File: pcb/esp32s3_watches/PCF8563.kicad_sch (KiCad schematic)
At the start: 1 part, among them U6 PCF8563TS

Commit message: BOM file updates. Scheme complete.
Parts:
- added BT400: BC2032-E2, esp32s3_watches:MPD_BC2032-E2, symbol esp32s3_watches:BC2032-E2
- added C400: 10uF, Capacitor_SMD:C_0805_2012Metric, symbol Device:C
- added C401: 100nF, Capacitor_SMD:C_0603_1608Metric, symbol Device:C
- added C402: 15pF, Capacitor_SMD:C_0603_1608Metric, symbol Device:C
- added D401, D402: 1N4148, Diode_SMD:D_SOD-123, symbol Device:D
- added R400, R401: 5k1R, Resistor_SMD:R_0805_2012Metric, symbol Device:R
- added Y400: 32768Hz, Crystal:Crystal_SMD_3225-4Pin_3.2x2.5mm, symbol Device:Crystal_GND24
- U400: renamed from U6; Manufacturer (none) -> NXP Semicon; Manufacturer Product Number (none) -> PCF8563TS/5,118
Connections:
- net +3.3V: now also C400.1, C401.1, D402.2 (A), R400.1, R401.1
- net GND: now also U400.2 (OSCO), U400.4 (VSS), BT400.N, C400.2, C401.2, C402.2, Y400.2, Y400.3, Y400.4
- net I2C_SCL: now also U400.6 (SCL), R401.2
- net I2C_SDA: now also U400.5 (SDA), R400.2
- net at U400.1 (OSCI): now also C402.1, Y400.1
- net PCF8563_INT: now reaches U400.3 (~{INT})
- net at U400.8 (VDD): now also D401.1 (K), D402.1 (K)
- new net: BT400.P, D401.2 (A)
- no-connect marks 0 -> 1
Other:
- moved on the sheet: U400

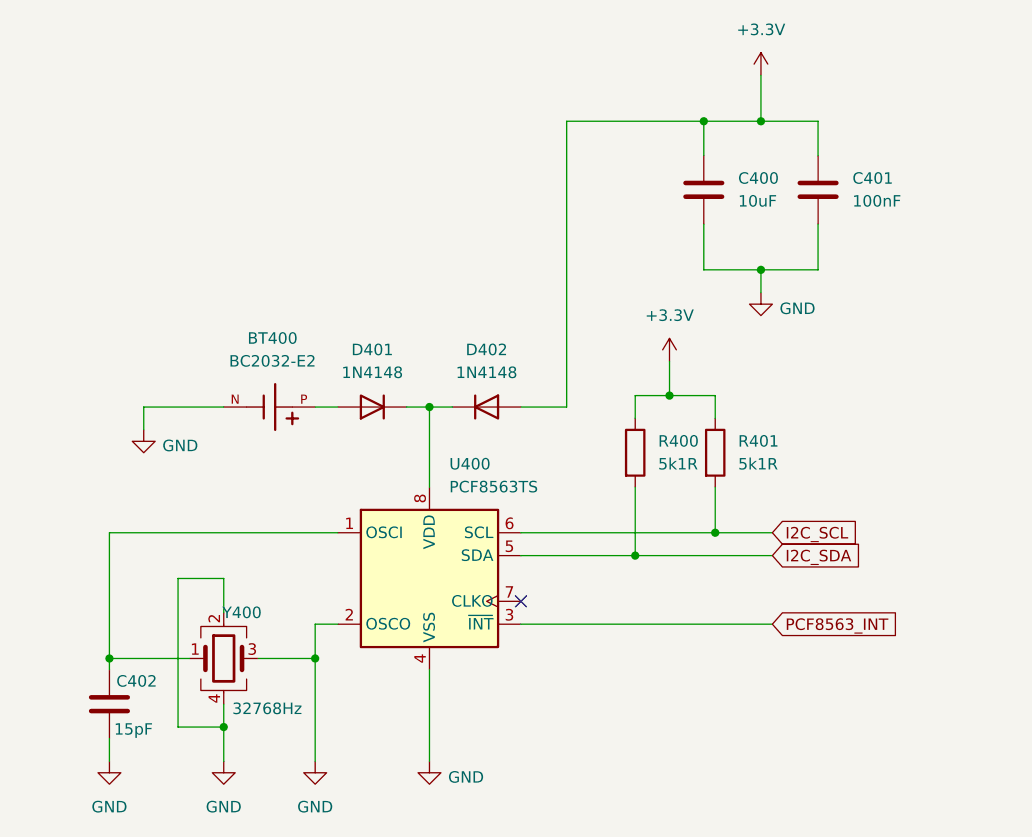
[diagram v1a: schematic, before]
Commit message: PCB initial layout
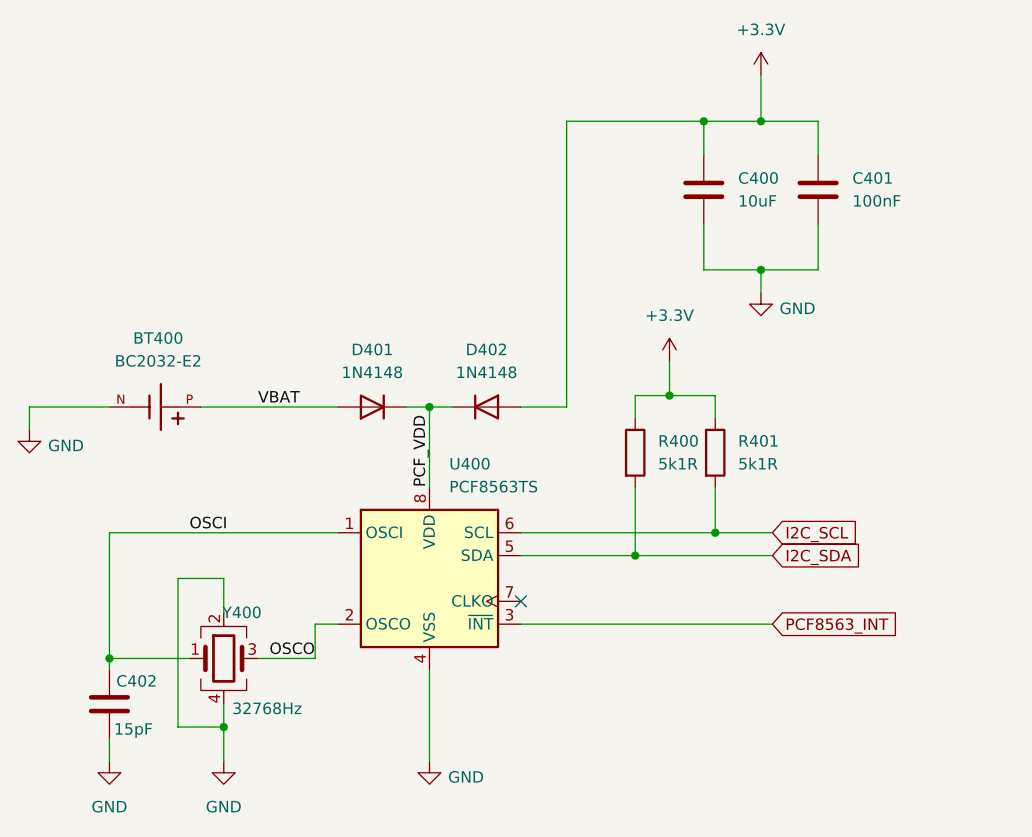
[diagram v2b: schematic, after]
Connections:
- net GND: no longer U400.2 (OSCO), Y400.3
- net VBAT: now reaches BT400.P, D401.2 (A)
- net PCF_VDD: now reaches D401.1 (K), D402.1 (K), U400.8 (VDD)
- net OSCI: now reaches C402.1, U400.1 (OSCI), Y400.1
- new net OSCO: U400.2 (OSCO), Y400.3
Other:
- moved on the sheet: BT400
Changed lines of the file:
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@@
-	)
-	(junction
-		(at 76.2 88.9)
-		(diameter 0)
-		(color 0 0 0 0)
 	)
 	(junction
@@
 	(wire
 		(pts
-			(xy 88.9 69.85) (xy 88.9 60.96)
+			(xy 88.9 60.96) (xy 88.9 69.85)
 		)
 		(stroke
@@
 	(wire
 		(pts
-			(xy 57.15 60.96) (xy 57.15 63.5)
+			(xy 44.45 60.96) (xy 44.45 63.5)
 		)
 		(stroke
@@
 	(wire
 		(pts
-			(xy 76.2 88.9) (xy 76.2 100.33)
-		)
-		(stroke
-			(width 0)
-			(type default)
-		)
-	)
-	(wire
-		(pts
 			(xy 125.73 48.26) (xy 125.73 45.72)
 		)
@@
 	(wire
 		(pts
-			(xy 66.04 60.96) (xy 57.15 60.96)
+			(xy 53.34 60.96) (xy 44.45 60.96)
 		)
 		(stroke
@@
 	(wire
 		(pts
-			(xy 76.2 60.96) (xy 78.74 60.96)
+			(xy 63.5 60.96) (xy 78.74 60.96)
 		)
 		(stroke
@@
 			(width 0)
 			(type default)
+		)
+	)
+	(label "PCF_VDD"
+		(at 88.9 69.85 90)
+		(effects
+			(font
+				(size 1.27 1.27)
+			)
+			(justify left bottom)
+		)
+	)
+	(label "OSCI"
+		(at 62.23 74.93 0)
+		(effects
+			(font
+				(size 1.27 1.27)
+			)
+			(justify left bottom)
+		)
+	)
+	(label "OSCO"
+		(at 71.12 88.9 0)
+		(effects
+			(font
+				(size 1.27 1.27)
+			)
+			(justify left bottom)
+		)
+	)
+	(label "VBAT"
+		(at 69.85 60.96 0)
+		(effects
+			(font
+				(size 1.27 1.27)
+			)
+			(justify left bottom)
 		)
 	)
@@
 	(symbol
 		(lib_id "esp32s3_watches:BC2032-E2")
-		(at 71.12 60.96 0)
+		(at 58.42 60.96 0)
 		(unit 1)
 		(exclude_from_sim no)
@@
 		(fields_autoplaced yes)
 		(property "Reference" "BT400"
-			(at 71.4629 53.34 0)
+			(at 58.7629 53.34 0)
 			(effects
 				(font
@@
 		)
 		(property "Value" "BC2032-E2"
-			(at 71.4629 55.88 0)
+			(at 58.7629 55.88 0)
 			(effects
 				(font
@@
 		)
 		(property "Footprint" "esp32s3_watches:MPD_BC2032-E2"
-			(at 71.12 60.96 0)
+			(at 58.42 60.96 0)
 			(effects
 				(font
@@
 		)
 		(property "Datasheet" ""
-			(at 71.12 60.96 0)
+			(at 58.42 60.96 0)
 			(effects
 				(font
@@
 		)
 		(property "Description" ""
-			(at 71.12 60.96 0)
+			(at 58.42 60.96 0)
 			(effects
 				(font
@@
 		)
 		(property "PARTREV" "D"
-			(at 71.12 60.96 0)
+			(at 58.42 60.96 0)
 			(effects
 				(font
@@
 		)
 		(property "STANDARD" "Manufacturer Recommendation"
-			(at 71.12 60.96 0)
+			(at 58.42 60.96 0)
 			(effects
 				(font
@@
 		)
 		(property "Manufacturer" "MYOUNG"
-			(at 71.12 60.96 0)
+			(at 58.42 60.96 0)
 			(effects
 				(font
@@
 		)
 		(property "Manufacturer Product Number" "BS-02-A1AJ010"
-			(at 71.12 60.96 0)
+			(at 58.42 60.96 0)
 			(effects
 				(font
@@
 	(symbol
 		(lib_id "power:GND")
-		(at 57.15 63.5 0)
+		(at 44.45 63.5 0)
 		(unit 1)
 		(exclude_from_sim no)
@@
 		(dnp no)
 		(property "Reference" "#PWR068"
-			(at 57.15 69.85 0)
+			(at 44.45 69.85 0)
 			(effects
 				(font
@@
 		)
 		(property "Value" "GND"
-			(at 61.214 65.278 0)
+			(at 48.514 65.278 0)
 			(effects
 				(font
@@
 		)
 		(property "Footprint" ""
-			(at 57.15 63.5 0)
+			(at 44.45 63.5 0)
 			(effects
 				(font
@@
 		)
 		(property "Datasheet" ""
-			(at 57.15 63.5 0)
+			(at 44.45 63.5 0)
 			(effects
 				(font
@@
 		)
 		(property "Description" "Power symbol creates a global label with name \"GND\" , ground"
-			(at 57.15 63.5 0)
+			(at 44.45 63.5 0)
 			(effects
 				(font
@@
 					(unit 1)
 				)
-			)
-		)
-	)
-	(symbol
-		(lib_id "power:GND")
-		(at 76.2 100.33 0)
-		(unit 1)
-		(exclude_from_sim no)
-		(in_bom yes)
-		(on_board yes)
-		(dnp no)
-		(fields_autoplaced yes)
-		(property "Reference" "#PWR067"
-			(at 76.2 106.68 0)
-			(effects
-				(font
-					(size 1.27 1.27)
-				)
-				(hide yes)
-			)
-		)
-		(property "Value" "GND"
-			(at 76.2 105.41 0)
-			(effects
-				(font
-					(size 1.27 1.27)
-				)
-			)
-		)
-		(property "Footprint" ""
-			(at 76.2 100.33 0)
-			(effects
-				(font
-					(size 1.27 1.27)
-				)
-				(hide yes)
-			)
-		)
-		(property "Datasheet" ""
-			(at 76.2 100.33 0)
-			(effects
-				(font
-					(size 1.27 1.27)
-				)
-				(hide yes)
-			)
-		)
-		(property "Description" "Power symbol creates a global label with name \"GND\" , ground"
-			(at 76.2 100.33 0)
-			(effects
-				(font
-					(size 1.27 1.27)
-				)
-				(hide yes)
-			)
-		)
-		(pin "1"
-		)
-		(instances
-			(project "esp32s3_watches"
-				(path "/546746d8-9087-4747-b922-4ea0efc98497/86d5c1be-317b-4ddb-a646-9d133da2ac94"
-					(reference "#PWR067")
-					(unit 1)
-				)
